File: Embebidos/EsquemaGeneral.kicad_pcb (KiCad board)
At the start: 2 copper layers, 100 x 99.9 mm, 79 parts, among them IC1 ESP32-WROVER-B__8MB_, J1 USB_A, J2 Conn_01x02, J3 RJ45, J4 RJ45, J5 Conn_02x06_Counter_Clockwise, J6 Conn_01x08, J7 Conn_01x04, Q1 BC847, Q2 BC847, Q3 BSS138, Q4 DMP3056LSDQ-13, Q5 BSS138, Q6 DMP3056LSDQ-13, SW1 SW_Reset, SW2 SW_Boot, U2 LM358, U3 SPX3819M5-L-3-3, U4 MIC29302WU, U5 MIC5219-3.3YM5

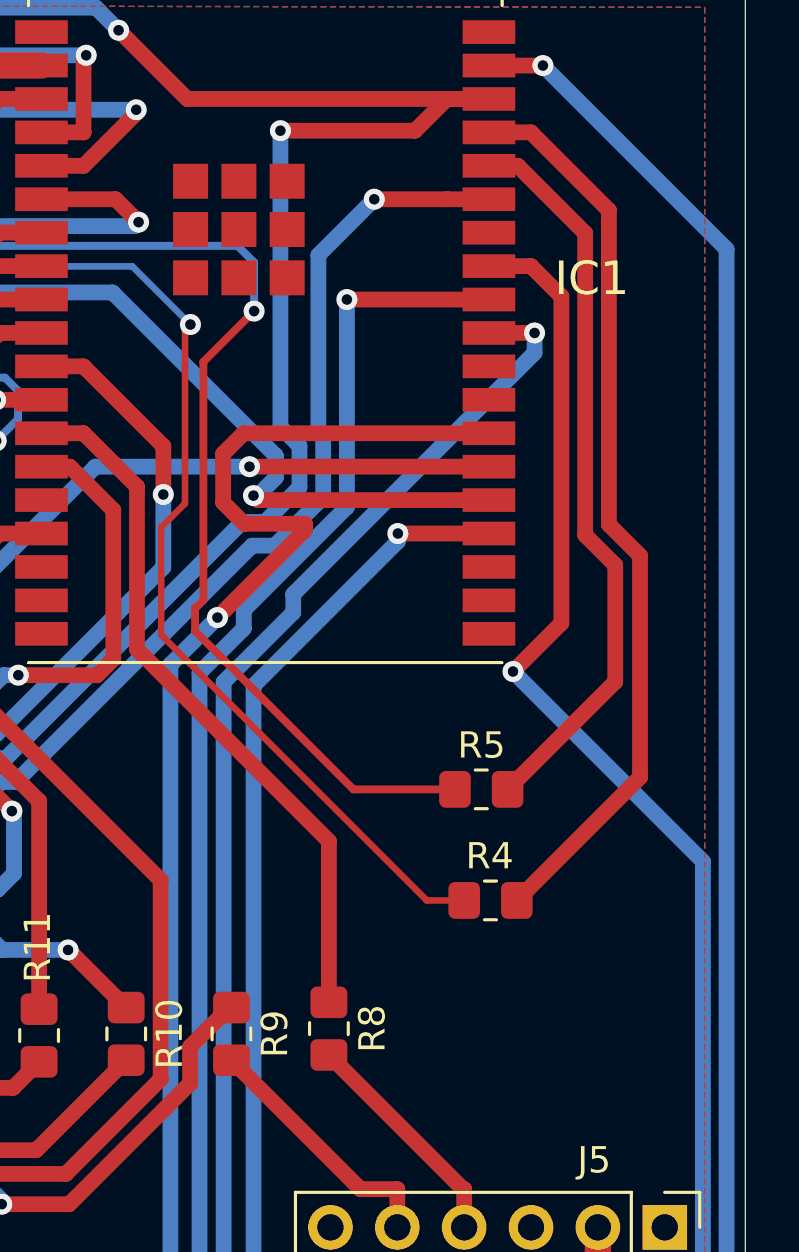
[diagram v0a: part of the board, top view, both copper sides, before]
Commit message: Pines programacon de emergencia
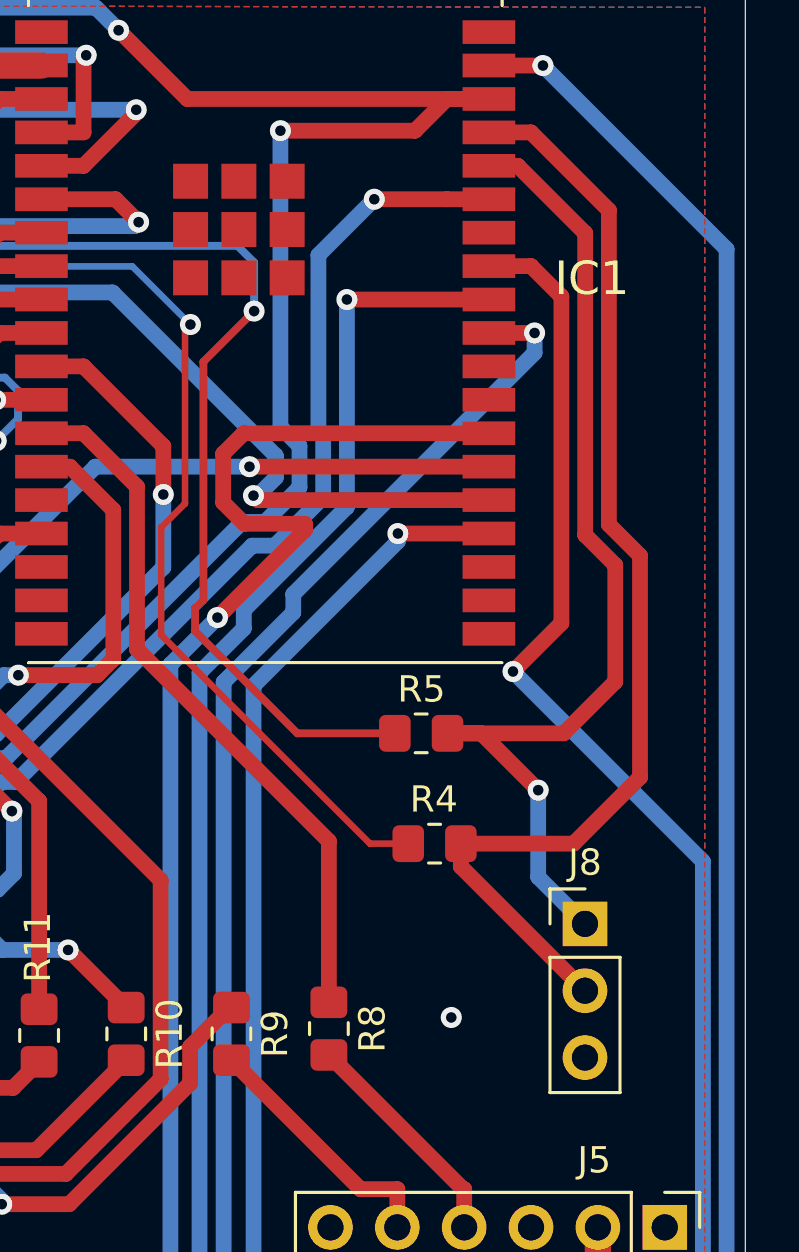
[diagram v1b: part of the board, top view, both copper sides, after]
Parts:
- added J8: Conn_01x03_Male, Connector_PinHeader_2.54mm:PinHeader_1x03_P2.54mm_Vertical, F.Cu at (171.4, 83.8)
- moved R5 3.12 mm to (165.2, 76.6)
- moved R4 3.03 mm to (165.7, 80.8)
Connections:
- net Net-(IC1-Pad34) renamed /Acondicionamiento/RX34
- net Net-(IC1-Pad35) renamed /Acondicionamiento/TX35
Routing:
- net /Acondicionamiento/RX34: track 28.0 -> 39.6 mm, vias 0 -> 1
- net /Acondicionamiento/TX35: track 34.4 -> 43.2 mm
- net /Acondicionamiento/RXCP: track 71.3 -> 68.1 mm
- net /Acondicionamiento/TXCP: track 70.8 -> 67.8 mm
- net GND: vias 51 -> 52

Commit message: Lista para los chinos
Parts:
- added H1: MountingHole, MountingHole:MountingHole_2.2mm_M2, F.Cu at (168.7, 111.9)
- added H2: MountingHole, MountingHole:MountingHole_2.2mm_M2, F.Cu at (81.5, 136.8)
- added H3: MountingHole, MountingHole:MountingHole_2.2mm_M2, F.Cu at (166.7, 87.1)
- added H4: MountingHole, MountingHole:MountingHole_2.2mm_M2, F.Cu at (81.8, 45.1)
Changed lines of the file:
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@@
     )
   )
+  (footprint "MountingHole:MountingHole_2.2mm_M2" (layer "F.Cu")
+    (at 81.85 45.13)
+    (descr "Mounting Hole 2.2mm, no annular, M2")
+    (tags "mounting hole 2.2mm no annular m2")
+    (property "Sheetfile" "EsquemaGeneral.kicad_sch")
+    (property "Sheetname" "")
+    (attr exclude_from_pos_files)
+    (fp_text reference "H4" (at 0 -3.2) (layer "F.SilkS")
+      (effects (font (size 1 1) (thickness 0.15)))
+    )
+    (fp_text value "MountingHole" (at 0 3.2) (layer "F.Fab")
+      (effects (font (size 1 1) (thickness 0.15)))
+    )
+    (fp_text user "${REFERENCE}" (at 0 0) (layer "F.Fab")
+      (effects (font (size 1 1) (thickness 0.15)))
+    )
+    (fp_circle (center 0 0) (end 2.2 0) (layer "Cmts.User") (width 0.15) (fill none))
+    (fp_circle (center 0 0) (end 2.45 0) (layer "F.CrtYd") (width 0.05) (fill none))
+    (pad "" np_thru_hole circle (at 0 0) (size 2.2 2.2) (drill 2.2) (layers *.Cu *.Mask))
+  )
   (footprint "Capacitor_SMD:C_0805_2012Metric_Pad1.18x1.45mm_HandSolder" (layer "F.Cu")
     (at 136.9825 51.61)
@@
     )
   )
+  (footprint "MountingHole:MountingHole_2.2mm_M2" (layer "F.Cu")
+    (at 81.54 136.83)
+    (descr "Mounting Hole 2.2mm, no annular, M2")
+    (tags "mounting hole 2.2mm no annular m2")
+    (property "Sheetfile" "EsquemaGeneral.kicad_sch")
+    (property "Sheetname" "")
+    (attr exclude_from_pos_files)
+    (fp_text reference "H2" (at 0 -3.2) (layer "F.SilkS")
+      (effects (font (size 1 1) (thickness 0.15)))
+    )
+    (fp_text value "MountingHole" (at 0 3.2) (layer "F.Fab")
+      (effects (font (size 1 1) (thickness 0.15)))
+    )
+    (fp_text user "${REFERENCE}" (at 0 0) (layer "F.Fab")
+      (effects (font (size 1 1) (thickness 0.15)))
+    )
+    (fp_circle (center 0 0) (end 2.2 0) (layer "Cmts.User") (width 0.15) (fill none))
+    (fp_circle (center 0 0) (end 2.45 0) (layer "F.CrtYd") (width 0.05) (fill none))
+    (pad "" np_thru_hole circle (at 0 0) (size 2.2 2.2) (drill 2.2) (layers *.Cu *.Mask))
+  )
   (footprint "Resistor_SMD:R_0805_2012Metric_Pad1.20x1.40mm_HandSolder" (layer "F.Cu")
     (at 124.74 67.73 -90)
@@
     )
   )
+  (footprint "MountingHole:MountingHole_2.2mm_M2" (layer "F.Cu")
+    (at 168.69 111.92)
+    (descr "Mounting Hole 2.2mm, no annular, M2")
+    (tags "mounting hole 2.2mm no annular m2")
+    (property "Sheetfile" "EsquemaGeneral.kicad_sch")
+    (property "Sheetname" "")
+    (attr exclude_from_pos_files)
+    (fp_text reference "H1" (at 0 -3.2) (layer "F.SilkS")
+      (effects (font (size 1 1) (thickness 0.15)))
+    )
+    (fp_text value "MountingHole" (at 0 3.2) (layer "F.Fab")
+      (effects (font (size 1 1) (thickness 0.15)))
+    )
+    (fp_text user "${REFERENCE}" (at 0 0) (layer "F.Fab")
+      (effects (font (size 1 1) (thickness 0.15)))
+    )
+    (fp_circle (center 0 0) (end 2.2 0) (layer "Cmts.User") (width 0.15) (fill none))
+    (fp_circle (center 0 0) (end 2.45 0) (layer "F.CrtYd") (width 0.05) (fill none))
+    (pad "" np_thru_hole circle (at 0 0) (size 2.2 2.2) (drill 2.2) (layers *.Cu *.Mask))
+  )
   (footprint "Resistor_SMD:R_0805_2012Metric_Pad1.20x1.40mm_HandSolder" (layer "F.Cu")
     (at 145.5484 78.44 -90)
@@
     )
   )
+  (footprint "MountingHole:MountingHole_2.2mm_M2" (layer "F.Cu")
+    (at 166.7 87.13)
+    (descr "Mounting Hole 2.2mm, no annular, M2")
+    (tags "mounting hole 2.2mm no annular m2")
+    (property "Sheetfile" "EsquemaGeneral.kicad_sch")
+    (property "Sheetname" "")
+    (attr exclude_from_pos_files)
+    (fp_text reference "H3" (at 0 -3.2) (layer "F.SilkS")
+      (effects (font (size 1 1) (thickness 0.15)))
+    )
+    (fp_text value "MountingHole" (at 0 3.2) (layer "F.Fab")
+      (effects (font (size 1 1) (thickness 0.15)))
+    )
+    (fp_text user "${REFERENCE}" (at 0 0) (layer "F.Fab")
+      (effects (font (size 1 1) (thickness 0.15)))
+    )
+    (fp_circle (center 0 0) (end 2.2 0) (layer "Cmts.User") (width 0.15) (fill none))
+    (fp_circle (center 0 0) (end 2.45 0) (layer "F.CrtYd") (width 0.05) (fill none))
+    (pad "" np_thru_hole circle (at 0 0) (size 2.2 2.2) (drill 2.2) (layers *.Cu *.Mask))
+  )
   (footprint "Connector_USB:USB_A_CNCTech_1001-011-01101_Horizontal" (layer "F.Cu")
     (at 120.81 43.49 90)
@@
   (via (at 133.67 120.7) (size 0.8) (drill 0.4) (layers "F.Cu" "B.Cu") (free) (net 2))
   (via (at 96.66 117.58) (size 0.8) (drill 0.4) (layers "F.Cu" "B.Cu") (free) (net 2))
-  (via (at 170.42 110.97) (size 0.8) (drill 0.4) (layers "F.Cu" "B.Cu") (free) (net 2))
+  (via (at 171.28 106.77) (size 0.8) (drill 0.4) (layers "F.Cu" "B.Cu") (free) (net 2))
   (via (at 96.6 79.57) (size 0.8) (drill 0.4) (layers "F.Cu" "B.Cu") (free) (net 2))
   (via (at 120.88 129.92) (size 0.8) (drill 0.4) (layers "F.Cu" "B.Cu") (free) (net 2))
@@
   (via (at 149.08 65.47) (size 0.8) (drill 0.4) (layers "F.Cu" "B.Cu") (free) (net 2))
   (via (at 106.16 62.91) (size 0.8) (drill 0.4) (layers "F.Cu" "B.Cu") (free) (net 2))
-  (via (at 83.33 46.11) (size 0.8) (drill 0.4) (layers "F.Cu" "B.Cu") (free) (net 2))
+  (via (at 84.47 52.06) (size 0.8) (drill 0.4) (layers "F.Cu" "B.Cu") (free) (net 2))
   (via (at 168.33 122.91) (size 0.8) (drill 0.4) (layers "F.Cu" "B.Cu") (free) (net 2))
   (via (at 116.98 64.32) (size 0.8) (drill 0.4) (layers "F.Cu" "B.Cu") (free) (net 2))
@@
   (via (at 103.67 94.98) (size 0.8) (drill 0.4) (layers "F.Cu" "B.Cu") (free) (net 2))
   (via (at 134.96 53.71) (size 0.8) (drill 0.4) (layers "F.Cu" "B.Cu") (free) (net 2))
-  (via (at 82.85 54.8) (size 0.8) (drill 0.4) (layers "F.Cu" "B.Cu") (free) (net 2))
+  (via (at 82.48 58.7) (size 0.8) (drill 0.4) (layers "F.Cu" "B.Cu") (free) (net 2))
   (via (at 85.68 106.74) (size 0.8) (drill 0.4) (layers "F.Cu" "B.Cu") (free) (net 2))
   (via (at 117.21 95.23) (size 0.8) (drill 0.4) (layers "F.Cu" "B.Cu") (free) (net 2))
@@
   (via (at 141.94 53.76) (size 0.8) (drill 0.4) (layers "F.Cu" "B.Cu") (free) (net 2))
   (via (at 141.82 95.47) (size 0.8) (drill 0.4) (layers "F.Cu" "B.Cu") (free) (net 2))
-  (via (at 166.37 87.376) (size 0.8) (drill 0.4) (layers "F.Cu" "B.Cu") (free) (net 2))
+  (via (at 169 91.37) (size 0.8) (drill 0.4) (layers "F.Cu" "B.Cu") (free) (net 2))
   (via (at 110.24 79.38) (size 0.8) (drill 0.4) (layers "F.Cu" "B.Cu") (free) (net 2))
   (via (at 114.89 111.57) (size 0.8) (drill 0.4) (layers "F.Cu" "B.Cu") (free) (net 2))

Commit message: para los chinos con logo
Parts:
- added :): LOGO, Logo:Logonuevo, B.Cu at (104.4, 86.4)
